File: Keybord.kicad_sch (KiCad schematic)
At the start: 1 part

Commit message: Add Neopix
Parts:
- added C13, C14: 10 uF, Capacitor_SMD:C_0402_1005Metric, symbol Device:C
- added J1: USB_C_Receptacle_USB2.0_14P, Connector_USB:USB_C_Receptacle_HRO_TYPE-C-31-M-12, symbol Connector:USB_C_Receptacle_USB2.0_14P
- added R1, R2: 5.1 K, Resistor_SMD:R_0402_1005Metric, symbol Device:R
- added U2: NCP1117-3.3_SOT223, Package_TO_SOT_SMD:SOT-223-3_TabPin2, symbol Regulator_Linear:NCP1117-3.3_SOT223
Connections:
- net PC13: now reaches U?.2 (PC13)
- net GND: now reaches U?.23 (VSS), U?.35 (VSS), U?.47 (VSS), U?.49 (VSS)
- net GND: now also U?.8 (VSSA), C13.2, C14.2, J1.A1 (GND), J1.A12 (GND), J1.B1 (GND), J1.B12 (GND), J1.S1 (SHIELD), R1.2, R2.2, U2.1 (GND)
- new net: J1.A5 (CC1), R1.1
- new net: J1.B5 (CC2), R2.1
- new net +3V3: C14.1, U2.2 (VO)
- new net USB_D+: J1.A6 (D+), J1.B6 (D+)
- new net USB_D-: J1.A7 (D-), J1.B7 (D-)
- new net VBUS: C13.1, J1.A4 (VBUS), J1.A9 (VBUS), J1.B4 (VBUS), J1.B9 (VBUS), U2.3 (VI)
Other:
- sheet Lights renamed LightsNeopix -OLD

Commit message: Finalilize the Keybord Shematic
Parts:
- added C?: 100nF, symbol Device:C
- added C?: 4.7uF, symbol Device:C
- added R? (x2): 10k, symbol Device:R
- added SW? (x2): SW_Push, symbol Switch:SW_Push
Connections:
- net +3V3: now also U?.1 (VBAT), U?.24 (VDD), U?.36 (VDD), U?.48 (VDD), U?.9 (VDDA), R?.1, SW?.1
- net GND: now also C?.1, C?.2, R?.2, SW?.1
- net USB_D+: now also U?.33 (PA12)
- net USB_D-: now also U?.32 (PA11)
- net PA0: now reaches U?.10 (PA0)
- net ROW0: now reaches U?.12 (PA2)
- net ROW1: now reaches U?.13 (PA3)
- net ROW2: now reaches U?.14 (PA4)
- net ROW3: now reaches U?.15 (PA5)
- net ROW4: now reaches U?.16 (PA6)
- net ROW5: now reaches U?.17 (PA7)
- net COL0: now reaches U?.18 (PB0)
- net COL1: now reaches U?.19 (PB1)
- net COL2: now reaches U?.20 (PB2)
- net COL10: now reaches U?.21 (PB10)
- net at U?.22 (VCAP1): now also C?.1
- net COL11: now reaches U?.25 (PB12)
- net COL12: now reaches U?.26 (PB13)
- net COL13: now reaches U?.27 (PB14)
- net COL3: now reaches U?.39 (PB3)
- net COL4: now reaches U?.40 (PB4)
- net COL5: now reaches U?.41 (PB5)
- net COL6: now reaches U?.42 (PB6)
- net COL7: now reaches U?.43 (PB7)
- net at U?.44 (BOOT0): now also R?.1, SW?.2
- net COL8: now reaches U?.45 (PB8)
- net COL9: now reaches U?.46 (PB9)
- net at U?.7 (NRST): now also C?.2, R?.2, SW?.2
- net PC13: no longer names the net of U?.2 (PC13)
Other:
- sheet LightsNeopix -OLD renamed LightsNeopix
- removed sheet Top
- note added: "62 Neopix - USB.2.0 Device max 6.40 mA per NeoPix ~ 10% Brightness"
- moved on the sheet: U?

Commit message: Start to fix ERC
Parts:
- gave numbers to parts that had none: 7

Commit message: Fixing. Add Footprints
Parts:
- added C4, C5, C6, C7, C8: 100nF, Capacitor_SMD:C_0603_1608Metric, symbol Device:C
- C1: footprint (none) -> Capacitor_SMD:C_0603_1608Metric
- C13, C14: footprint Capacitor_SMD:C_0402_1005Metric -> Capacitor_SMD:C_0805_2012Metric
- C2: footprint (none) -> Capacitor_SMD:C_0805_2012Metric
- R3, R4: footprint (none) -> Resistor_SMD:R_0603_1608Metric
- SW2, SW3: footprint (none) -> JonasLib-Git:smd_switch_sunrom4388
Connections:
- net +3V3: now also C4.2, C5.2, C6.2, C7.2, C8.2; no longer U1.1 (VBAT), U1.24 (VDD), U1.36 (VDD), U1.48 (VDD), U1.9 (VDDA)
- new net: C4.1, U1.1 (VBAT)
- new net: C7.1, U1.48 (VDD)
- new net: C8.1, U1.9 (VDDA)
- new net: C6.1, U1.36 (VDD)
- new net: C5.1, U1.24 (VDD)

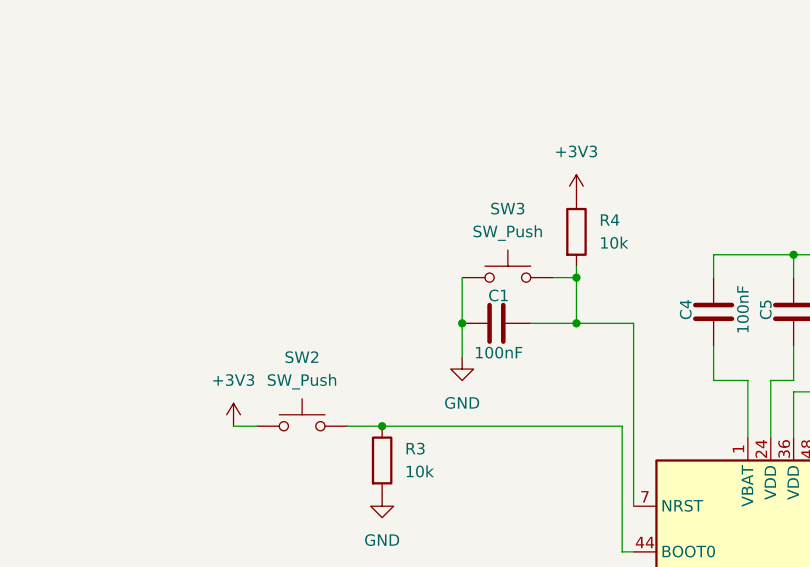
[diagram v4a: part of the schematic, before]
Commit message: Switch Layout on PCB
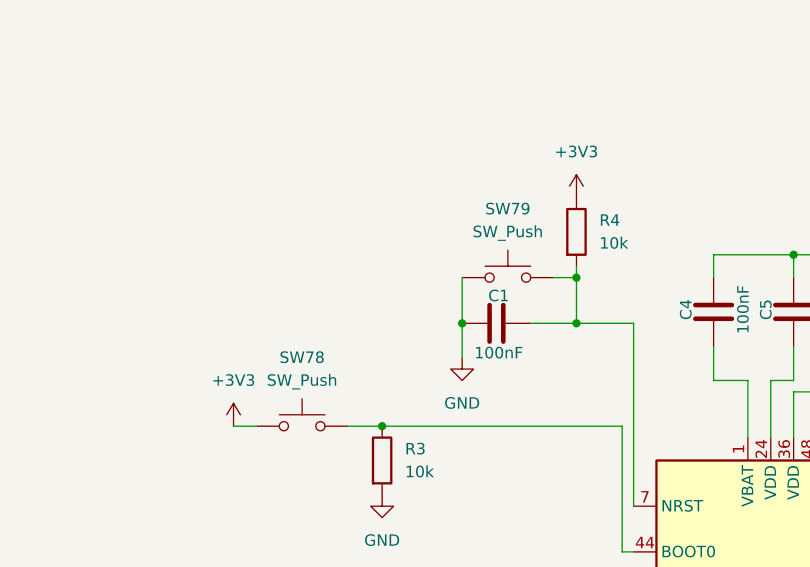
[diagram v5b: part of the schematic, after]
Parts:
- renumbered SW2 to SW78, SW3 to SW79
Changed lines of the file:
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@@
 		(dnp no)
 		(fields_autoplaced yes)
-		(property "Reference" "SW3"
+		(property "Reference" "SW79"
 			(at 76.2 40.64 0)
 			(effects
@@
 			(project ""
 				(path "/e528f1ae-3ae1-474a-b1e2-6cda2df874b7"
-					(reference "SW3")
+					(reference "SW79")
 					(unit 1)
 				)
@@
 		(dnp no)
 		(fields_autoplaced yes)
-		(property "Reference" "SW2"
+		(property "Reference" "SW78"
 			(at 53.34 57.15 0)
 			(effects
@@
 			(project ""
 				(path "/e528f1ae-3ae1-474a-b1e2-6cda2df874b7"
-					(reference "SW2")
-					(unit 1)
-				)
+					(reference "SW78")
+					(unit 1)
+				)
